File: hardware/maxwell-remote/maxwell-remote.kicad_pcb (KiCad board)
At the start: 2 copper layers, 71.1 x 38.1 mm, 28 parts, among them J2 UART, J3 FPC 1, J4 FPC 2, J5 Programmer, J6 B0_JMP, J7 B1_JMP, J9 ESP_BM, U1 STM32F103C8Tx, U2 ESP32-WROOM, Y1 Crystal, Y2 Crystal_GND23

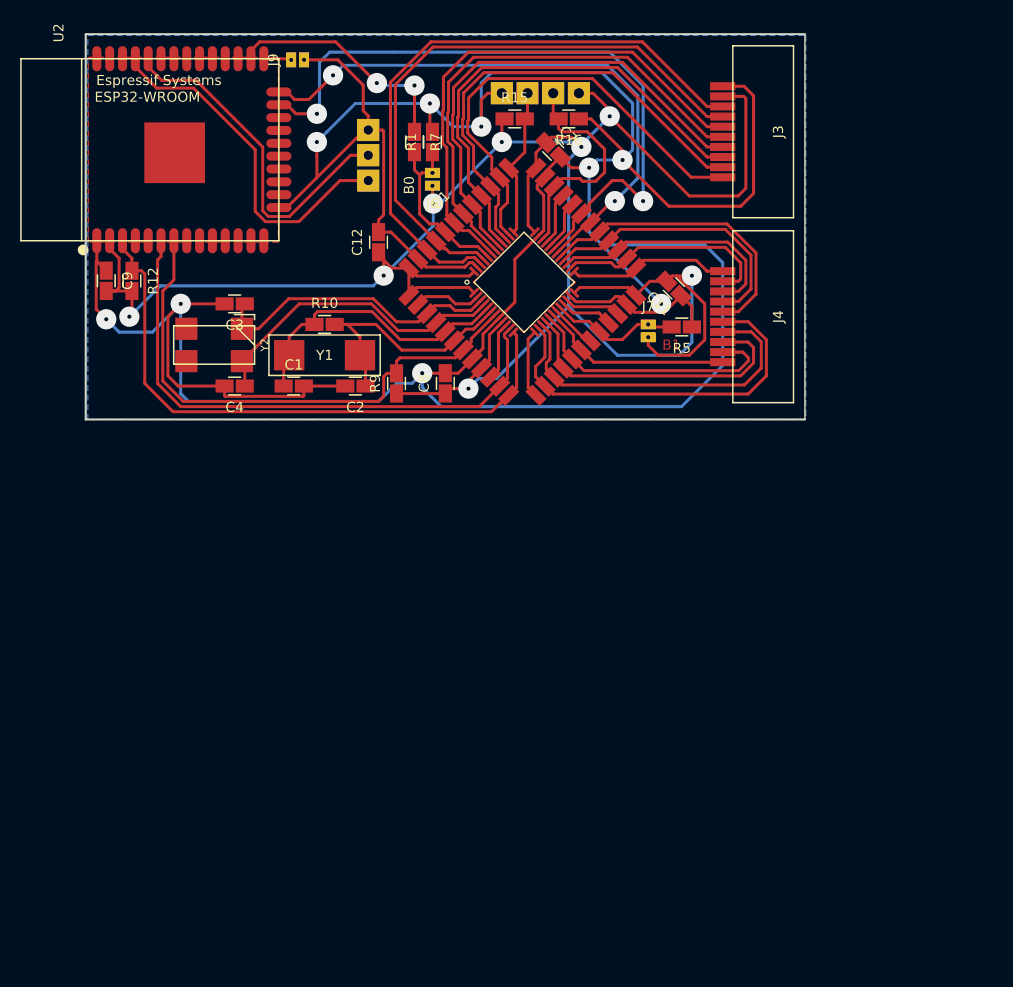
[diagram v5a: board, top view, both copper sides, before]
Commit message: Maxwell Remote v2.0
* Adds WAKE-controlled power switch to save power while sleeping.
* Uses pin headers for connecting upper and lower layers instead
  of FPC connectors.
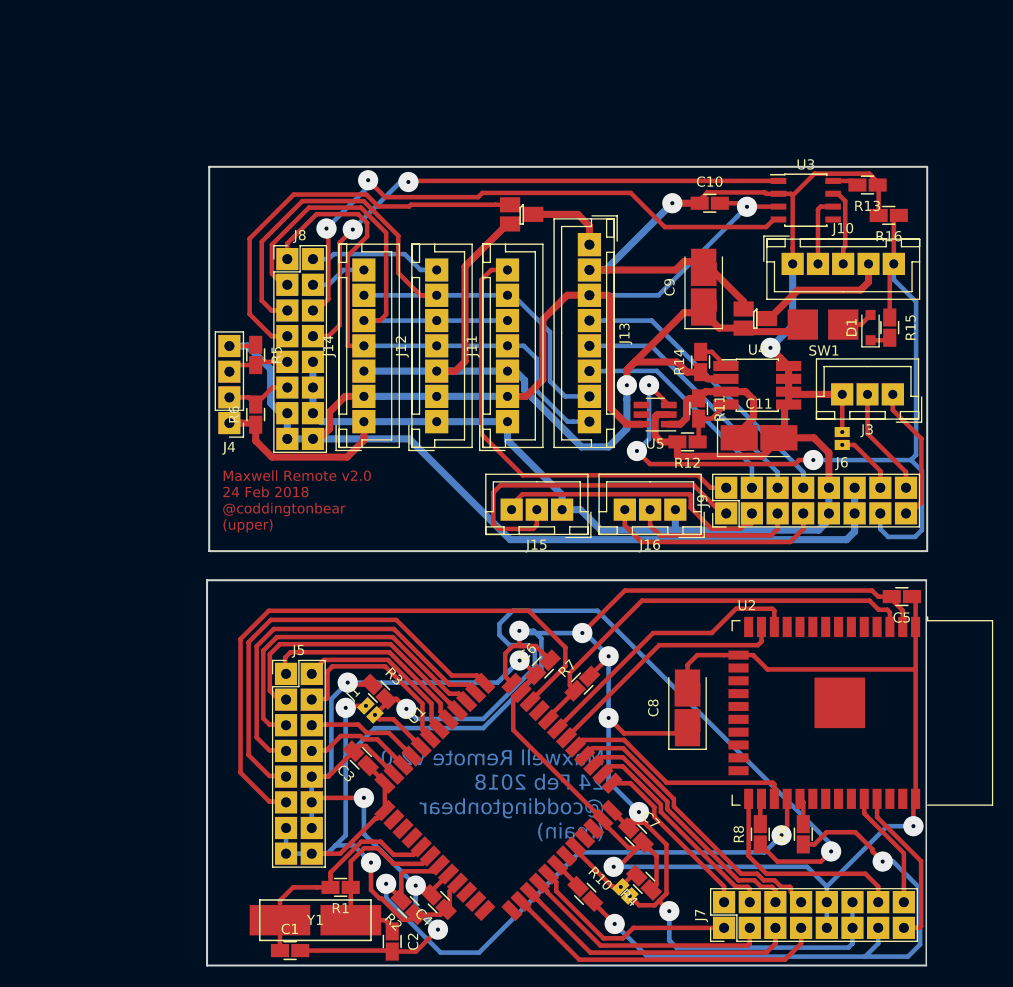
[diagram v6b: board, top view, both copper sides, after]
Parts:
- removed C12: 0.1, coddingtonbear/coddingtonbear.pretty:0805_Milling
- removed Y2: Crystal_GND23, coddingtonbear:SM-CRYSTAL-ABS25_LargePads
- added C10: 0.1u, coddingtonbear:0805_Milling, F.Cu at (159.5, 72.6)
- added C5: 0.1u, coddingtonbear:0805_Milling, F.Cu at (178.5, 111.5)
- added C6: 0.1u, coddingtonbear:0805_Milling, F.Cu at (143.0, 118.5)
- added D1: 1N4148WS, Diode_SMD:D_SOD-323_HandSoldering, F.Cu at (175.4, 84.9)
- added J1: BOOT0, coddingtonbear:Pin_Header_Straight_1x02_Pitch1.27mm_JMP, F.Cu at (125.5, 122.3)
- added J10: CAN, coddingtonbear:JST_XH_B05B-XH-A_05x2.50mm_Straight_LargePads, F.Cu at (167.7, 78.6)
- added J11: SPI1_C, coddingtonbear:JST_XH_B07B-XH-A_07x2.50mm_Straight_LargePads, F.Cu at (139.5, 94.2)
- added J12: SPI1_B, coddingtonbear:JST_XH_B07B-XH-A_07x2.50mm_Straight_LargePads, F.Cu at (132.5, 94.2)
- added J13: Display, coddingtonbear:JST_XH_B08B-XH-A_08x2.50mm_Straight_LargePads, F.Cu at (147.6, 76.7)
- added J14: SPI1_A, coddingtonbear:JST_XH_B07B-XH-A_07x2.50mm_Straight_LargePads, F.Cu at (125.3, 94.2)
- added J15: Left, coddingtonbear:JST_XH_B03B-XH-A_03x2.50mm_Straight_LargePads, F.Cu at (144.9, 102.9)
- added J16: Right, coddingtonbear:JST_XH_B03B-XH-A_03x2.50mm_Straight_LargePads, F.Cu at (156.1, 102.9)
- added J8: Upper-Left, coddingtonbear:PinHeader_2x08_P2.54mm_Vertical_LargePads, F.Cu at (117.7, 78.1)
- added Q1: NTR1P02TI, coddingtonbear:SOT-23_LargePads, F.Cu at (164.0, 84.0)
- added Q2: NTR1P02TI, coddingtonbear:SOT-23_LargePads, F.Cu at (140.9, 73.7)
- added R11: 60k, coddingtonbear:0805_Milling, F.Cu at (158.4, 92.9)
- added R13: 10k, coddingtonbear:0805_Milling, F.Cu at (175.1, 70.8)
- added R14: 10k, coddingtonbear:0805_Milling, F.Cu at (158.6, 88.3)
- added R2: 10k, coddingtonbear:0805_Milling, F.Cu at (129.7, 142.2)
- added R3: 100k, coddingtonbear:0805_Milling, F.Cu at (126.8, 120.9)
- added R4: 100k, coddingtonbear:0805_Milling, F.Cu at (153.0, 139.8)
- added R6: 10k, coddingtonbear:0805_Milling, F.Cu at (114.6, 93.5)
- added R8: 300, coddingtonbear:0805_Milling, F.Cu at (164.5, 135.0)
- added SW1: SW_Push, coddingtonbear:SMD_MINI_BLACK_TACTILE_SWITCH, F.Cu at (170.7, 84.6)
- added U3: SN65HVD235, Package_SO:SOIC-8_3.9x4.9mm_P1.27mm, F.Cu at (169.0, 72.3)
- added U4: MIC5209-ADJ, coddingtonbear:SOIC-8_3.9x4.9mm_P1.27mm_LargePads, F.Cu at (164.2, 90.6)
- added U5: TPS22917, Package_TO_SOT_SMD:SOT-23-6_Handsoldering, F.Cu at (154.1, 93.5)
- C1, C2, R16: footprint coddingtonbear/coddingtonbear.pretty:0805_Milling -> coddingtonbear:0805_Milling
- C11: value 0.1 -> 2.2u; footprint coddingtonbear/coddingtonbear.pretty:0805_Milling -> coddingtonbear:CP_Tantalum_Case-C_EIA-6032-28_Milling
- C3, C4: value 22p -> 0.1u; footprint coddingtonbear/coddingtonbear.pretty:0805_Milling -> coddingtonbear:0805_Milling
- C7: value 0.1 -> 0.1u; footprint coddingtonbear/coddingtonbear.pretty:0805_Milling -> coddingtonbear:0805_Milling
- C8: value 0.1 -> 220u; footprint coddingtonbear/coddingtonbear.pretty:0805_Milling -> coddingtonbear:CP_Tantalum_Case-C_EIA-6032-28_Milling
- C9: value 0.1 -> 100u; footprint coddingtonbear/coddingtonbear.pretty:0805_Milling -> coddingtonbear:CP_Tantalum_Case-C_EIA-6032-28_Milling
- J2: value UART -> BOOT1; footprint coddingtonbear:JST_XH_B03B-XH-A_03x2.50mm_Straight_LargePads -> coddingtonbear:Pin_Header_Straight_1x02_Pitch1.27mm_JMP
- J3: value FPC 1 -> ESPUART; footprint coddingtonbear/coddingtonbear.pretty:10P_FPC_1.0mm -> coddingtonbear:JST_XH_B03B-XH-A_03x2.50mm_Straight_LargePads
- J4: value FPC 2 -> PROG; footprint coddingtonbear/coddingtonbear.pretty:10P_FPC_1.0mm -> coddingtonbear:Pin_Header_Straight_1x04_Pitch2.54mm_LargePads
- J5: value Programmer -> Lower-Left; footprint coddingtonbear/coddingtonbear.pretty:Pin_Header_Straight_1x04_Pitch2.54mm_LargePads -> coddingtonbear:PinHeader_2x08_P2.54mm_Vertical_LargePads; moved to F.Cu
- J6: value B0_JMP -> ESPBOOT; footprint coddingtonbear/coddingtonbear.pretty:Pin_Header_Straight_1x02_Pitch1.27mm_JMP -> coddingtonbear:Pin_Header_Straight_1x02_Pitch1.27mm_JMP
- J7: value B1_JMP -> Lower-Right; footprint coddingtonbear/coddingtonbear.pretty:Pin_Header_Straight_1x02_Pitch1.27mm_JMP -> coddingtonbear:PinHeader_2x08_P2.54mm_Vertical_LargePads
- J9: value ESP_BM -> Upper-Right; footprint coddingtonbear/coddingtonbear.pretty:Pin_Header_Straight_1x02_Pitch1.27mm_JMP -> coddingtonbear:PinHeader_2x08_P2.54mm_Vertical_LargePads
- R1: value 100k -> 1M; footprint coddingtonbear/coddingtonbear.pretty:0805_Milling -> coddingtonbear:0805_Milling
- R10: value 1M -> 300; footprint coddingtonbear/coddingtonbear.pretty:0805_Milling -> coddingtonbear:0805_Milling
- R12: value 10k -> 100k; footprint coddingtonbear/coddingtonbear.pretty:0805_Milling -> coddingtonbear:0805_Milling
- R15, R9: value 10k -> 300; footprint coddingtonbear/coddingtonbear.pretty:0805_Milling -> coddingtonbear:0805_Milling
- R5: value 100k -> 10k; footprint coddingtonbear/coddingtonbear.pretty:0805_Milling -> coddingtonbear:0805_Milling
- R7: value 330 -> 10k; footprint coddingtonbear/coddingtonbear.pretty:0805_Milling -> coddingtonbear:0805_Milling
- U1: value STM32F103C8Tx -> STM32F103CBTx; footprint kicad-castellated-breakouts:QFP48-1.27MM-CASTELLATED-VERS -> castellated-breakouts:QFP48-1.27MM-CASTELLATED
- U2: value ESP32-WROOM -> ESP32-WROOM-32; footprint NorbotNorway/NorBotKiCadFootprints.pretty:ESP32-WROOM -> RF_Module:ESP32-WROOM-32
- Y1: value Crystal -> 8M; footprint cpavlina/kicad-pcblib/smd-non-ipc.pretty:Abracon-ABM2 -> coddingtonbear:Abracon-ABM2_LargePads
- moved U2 87.5 mm to (171.6, 123.0)
- moved R1 74.3 mm to (123.0, 140.2), turned to 180 degrees
- moved J2 74.2 mm to (150.7, 140.2), turned to 225 degrees
- moved C7 68.3 mm to (152.2, 135.1)
- moved J5 64.3 mm to (117.6, 119.1), turned to 0 degrees
- moved J9 62.1 mm to (161.1, 103.3)
- moved R10 61.9 mm to (147.2, 140.9), turned to 315 degrees
- moved J7 60.1 mm to (160.9, 144.3), turned to 90 degrees
- moved R9 60.0 mm to (168.8, 135.0)
- moved C9 59.1 mm to (158.9, 80.9), turned to 90 degrees
- moved R12 57.2 mm to (157.3, 96.2), turned to 180 degrees
- moved R7 56.1 mm to (146.9, 120.1), turned to 45 degrees
- moved Y1 55.9 mm to (120.5, 143.5), turned to 0 degrees
- moved C1 55.8 mm to (118.0, 146.5)
- moved C2 55.0 mm to (128.1, 145.6), turned to 270 degrees
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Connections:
- C1 pad 2: GND -> GND_A
- C11 pad 1: GND -> +3V3_U
- C11 pad 2: +3V3 -> GND_B
- C2 pad 2: GND -> GND_A
- C3 pad 1: Net-(C3-Pad1) -> +3V3_A
- C3 pad 2: GND -> GND_A
- C4 pad 1: Net-(C4-Pad1) -> +3V3_A
- C4 pad 2: GND -> GND_A
- C7 pad 1: +3V3 -> +3V3_A
- C7 pad 2: GND -> GND_A
- C8 pad 1: +3V3 -> +3V3_A
- C8 pad 2: GND -> GND_A
- C9 pad 1: GND -> +BATT
- C9 pad 2: +3V3 -> GND_B
- J2 pad 1: BT_OUT -> BOOT1
- J2 pad 2: BT_IN -> +3V3_A
- J3 pad 1: GND -> ESP_DO_U
- J3 pad 2: +3V3 -> ESP_DI_U
- J3 pad 3: CAN_TX -> GND_B
- J4 pad 1: ~SPI_CS_4 -> GND_B
- J4 pad 2: SCREEN_A0 -> SWDIO_U
- J4 pad 3: ~SCREEN_RST -> SWCLK_U
- J4 pad 4: ~SCREEN_CS -> +3V3_B
- J5 pad 1: +3V3 -> SPI1_MOSI
- J5 pad 2: SWDIO -> ~SPI1_CS_3
- J5 pad 3: SWCLK -> SPI1_MISO
- J5 pad 4: GND -> ~SPI1_CS_2
- J6 pad 1: +3V3 -> ESP_BOOT_MODE_U
- J6 pad 2: BOOT0 -> GND_B
- J7 pad 1: BOOT1 -> ~LEFT_A
- J7 pad 2: +3V3 -> ~SPI_CS_4
- J9 pad 1: ESP_BOOT_MODE -> LEFT_A_U
- J9 pad 2: GND -> ~SPI1_CS_4_U
- R1 pad 1: BOOT0 -> Net-(C2-Pad1)
- R1 pad 2: GND -> Net-(C1-Pad1)
- R10 pad 1: Net-(C1-Pad1) -> Net-(R10-Pad1)
- R10 pad 2: Net-(C2-Pad1) -> ESP_AVAILABLE
- R12 pad 1: DISBABLE_BLUETOOTH_ -> Net-(R11-Pad2)
- R12 pad 2: +3V3 -> GND_B
- R15 pad 1: +3V3 -> ESP_AVAILABLE_U
- R15 pad 2: SWCLK -> Net-(D1-Pad1)
- R16 pad 1: GND -> ESP_AVAILABLE_U
- R16 pad 2: SWDIO -> GND_B
- R5 pad 1: GND -> +3V3_B
- R5 pad 2: BOOT1 -> SWCLK_U
- R7 pad 1: Net-(R7-Pad1) -> DISBABLE_BLUETOOTH_
- R7 pad 2: BOOT0 -> +3V3_A
- R9 pad 1: +3V3 -> ESP_AVAILABLE
- R9 pad 2: NRST -> Net-(R9-Pad2)
- U1 pad 1: +3V3 -> +3V3_A
- U1 pad 11: BT_KEY -> Net-(U1-Pad11)
- U1 pad 12: DISBABLE_BLUETOOTH_ -> Net-(U1-Pad12)
- U1 pad 18: WAKE -> Net-(R10-Pad1)
- U1 pad 23: GND -> GND_A
- U1 pad 24: +3V3 -> +3V3_A
- U1 pad 29: ~ENABLE_CAN -> BT_KEY
- U1 pad 3: Net-(C3-Pad1) -> Net-(U1-Pad3)
- U1 pad 30: MC_OUT -> BT_DI
- U1 pad 31: MC_IN -> BT_DO
- U1 pad 32: Net-(U1-Pad32) -> DISBABLE_BLUETOOTH_
- U1 pad 35: GND -> GND_A
- U1 pad 36: +3V3 -> +3V3_A
- U1 pad 4: Net-(C4-Pad1) -> Net-(U1-Pad4)
- U1 pad 47: GND -> GND_A
- U1 pad 48: +3V3 -> +3V3_A
- U1 pad 8: GND -> GND_A
- U1 pad 9: +3V3 -> +3V3_A
- U2 pad 1: GND -> GND_A
- U2 pad 12: Net-(U2-Pad12) -> BT_DO
- U2 pad 13: Net-(U2-Pad13) -> BT_DI
- U2 pad 15: GND -> GND_A
- U2 pad 2: +3V3 -> +3V3_A
- U2 pad 23: MC_IN -> Net-(U2-Pad23)
- U2 pad 24: MC_OUT -> Net-(U2-Pad24)
- U2 pad 26: Net-(R7-Pad1) -> Net-(R8-Pad2)
- U2 pad 27: Net-(U2-Pad27) -> BT_KEY
- U2 pad 28: Net-(U2-Pad28) -> NRST
- U2 pad 29: Net-(U2-Pad29) -> Net-(R9-Pad2)
- U2 pad 34: BT_IN -> ESP_DI
- U2 pad 35: BT_OUT -> ESP_DO
- U2 pad 38: GND -> GND_A
- U2 pad 39: GND -> (no net)
- U2 pad 6: BT_KEY -> Net-(U2-Pad6)
- U2 pad 7: NRST -> Net-(U2-Pad7)
- Y1 pad 1: Net-(C2-Pad1) -> Net-(C1-Pad1)
- Y1 pad 2: Net-(C1-Pad1) -> Net-(C2-Pad1)
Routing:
- net GND: track 350.5 -> 0.00 mm, vias 9 -> 0
- net +3V3: track 236.7 -> 0.00 mm, vias 8 -> 0
- net +3V3_A: track 0.00 -> 215.8 mm, vias 0 -> 8
- net GND_A: track 0.00 -> 209.6 mm, vias 0 -> 7
- net GND_B: track 0.00 -> 203.1 mm, vias 0 -> 2
- net +3V3_B: track 0.00 -> 160.2 mm, vias 0 -> 1
- net +BATT: track 0.00 -> 86.4 mm, vias 0 -> 1
- net ESP_AVAILABLE_U: track 0.00 -> 82.6 mm, vias 0 -> 3
- net MC_IN: track 67.7 -> 0.00 mm, vias 2 -> 0
- net BOOT0: track 18.3 -> 84.2 mm, vias 0 -> 2
- net SPI1_SCK_U: track 0.00 -> 63.0 mm
- net ESP_AVAILABLE: track 0.00 -> 58.8 mm, vias 0 -> 2
- net CAN_RX_U: track 0.00 -> 58.7 mm, vias 0 -> 2
- net MC_OUT: track 57.8 -> 0.00 mm, vias 2 -> 0
- net CAN_TX_U: track 0.00 -> 57.2 mm, vias 0 -> 2
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- removed copper zone on B.Cu, net GND
- removed copper zone on F.Cu, net GND
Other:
- board size 71.1 x 38.1 mm -> 71.2 x 79 mm
- net class Default: trace_width 0.3 -> 0.45
- board text added: "Maxwell Remote v2.0 24 Feb 2018 @coddingtonbear (main)"
- board text added: "Maxwell Remote v2.0 24 Feb 2018 @coddingtonbear (upper)"
- board text removed: "+"
- board text removed: "-"
- board text removed: "B0"
- board text removed: "B1"
- board text removed: "C"
- board text removed: "IO"
- board text removed: "RX"
- board text removed: "TX"
- board text removed: "_"
- board text removed: "maxwell-remote v5.0 @coddingtonbear 24 June 2018"

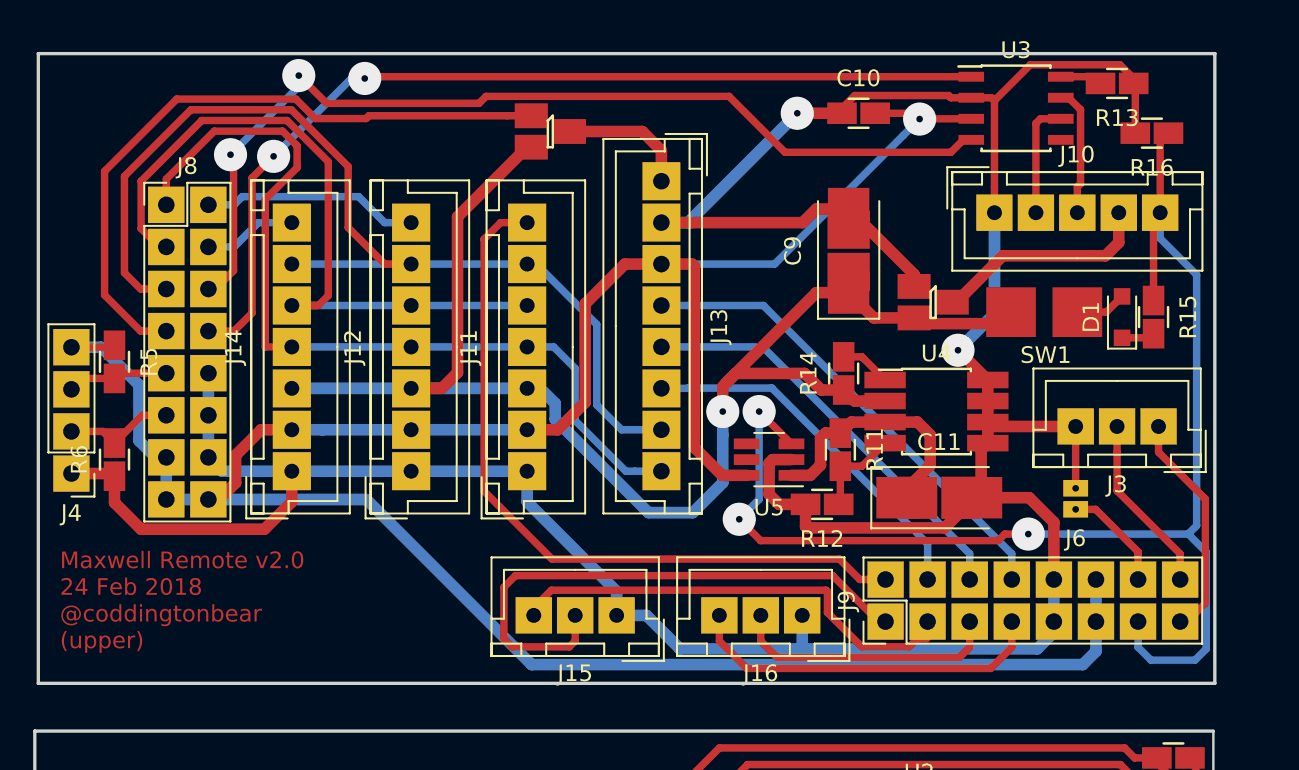
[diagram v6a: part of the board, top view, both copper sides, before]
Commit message: Maxwell Remote v2.0.1
* Adds support for power-on by pressing handlebar button.
  The earlier design relied on the microcontroller waking
  when the button was pressed, but in this new switch
  configuration the microcontroller won't even be powered
  while the device is asleep, so we need to hard-wire
  the power button to the WAKE line.
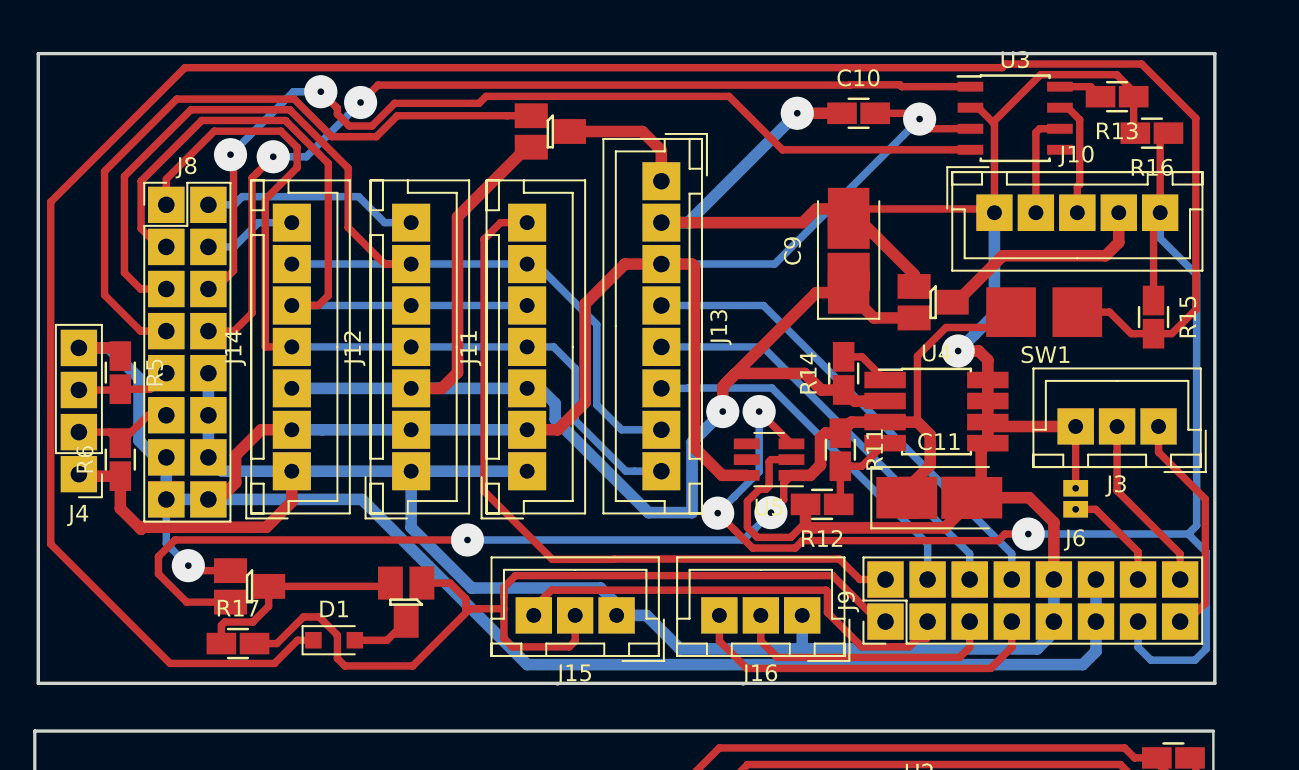
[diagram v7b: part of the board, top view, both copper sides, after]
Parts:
- added Q3: NTR1P02TI, coddingtonbear:SOT-23_LargePads, F.Cu at (122.8, 101.2)
- added Q4: NTR1P02TI, coddingtonbear:SOT-23_LargePads, F.Cu at (132.2, 102.1)
- added R17: 10k, coddingtonbear:0805_Milling, F.Cu at (122.0, 104.6)
- moved D1 51.4 mm to (127.8, 104.4), turned to 0 degrees
- moved R13 0.80 mm to (175.1, 71.6)
- moved R5 0.74 mm to (115.0, 88.2)
- moved U3 0.60 mm to (168.9, 72.9)
- moved J4 0.45 mm to (112.5, 94.4)
- moved R6 0.35 mm to (115.0, 93.5)
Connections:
- SW1 pad 1: +BATT -> +3V3_U
- SW1 pad 2: Net-(D1-Pad2) -> Net-(D1-Pad1)
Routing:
- net Net-(D1-Pad1): track 2.00 -> 133.8 mm
- net +3V3_U: track 15.6 -> 73.3 mm, vias 0 -> 2
- net LEFT_A_U: track 33.8 -> 56.9 mm
- net Net-(Q3-Pad3): track 0.00 -> 13.1 mm
- net GND_B: track 203.1 -> 215.7 mm
- net +3V3_B: track 160.2 -> 167.4 mm, vias 1 -> 2
- net +BATT: track 86.4 -> 80.1 mm
- net ESP_AVAILABLE_U: track 82.6 -> 84.6 mm
- net ~ENABLE_SCREEN_U: track 40.2 -> 41.1 mm
- net Net-(J10-Pad3): track 7.79 -> 7.17 mm
- net Net-(J10-Pad2): track 7.00 -> 6.38 mm
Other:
- board text removed: "Maxwell Remote v2.0 24 Feb 2018 @coddingtonbear (upper)"

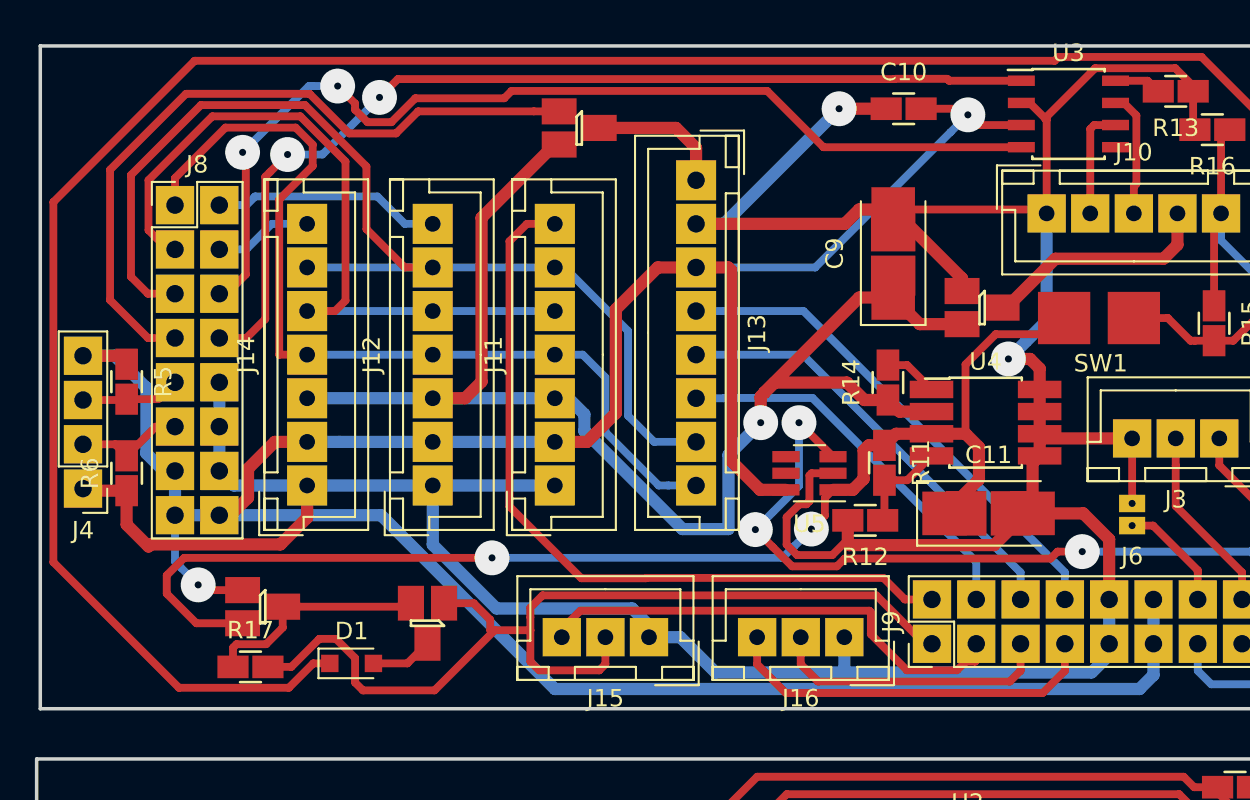
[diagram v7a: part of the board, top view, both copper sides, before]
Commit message: Maxwell Remote v2.0.2
* Switches off power to SPI-connected devices when powered-down.
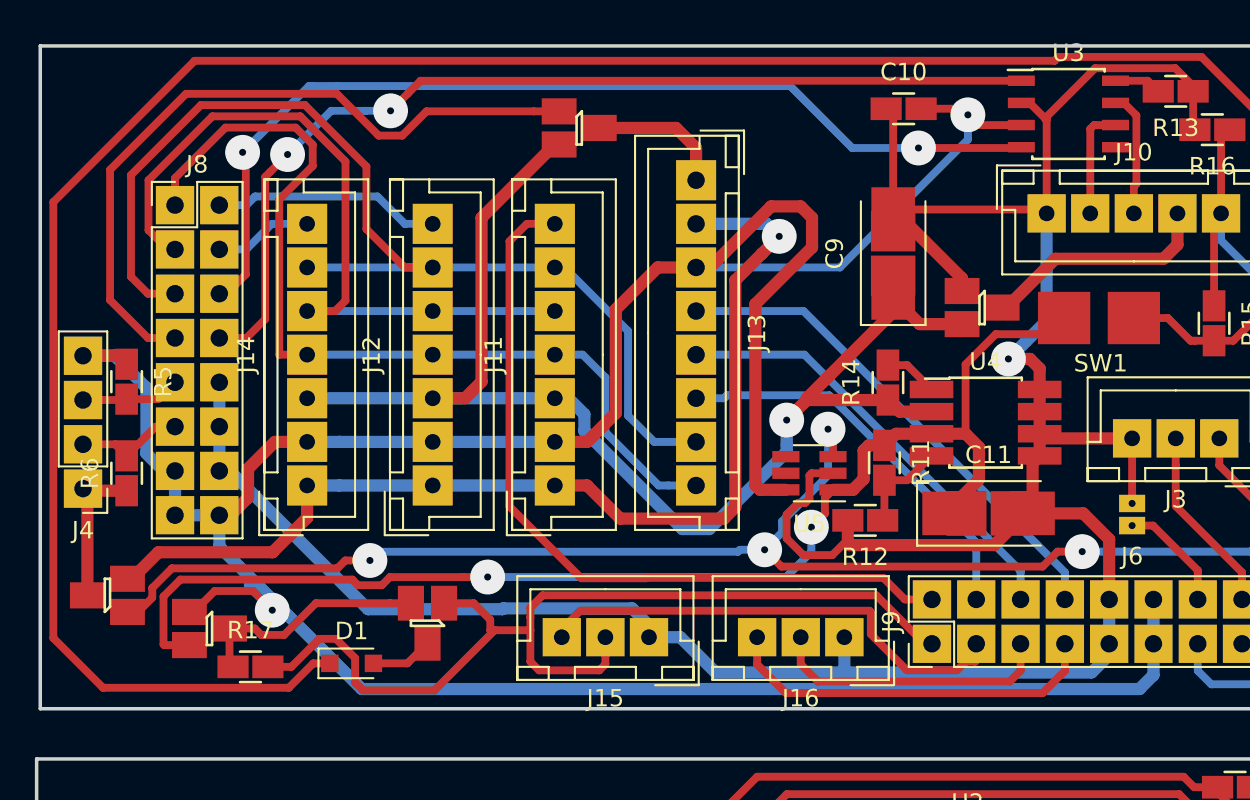
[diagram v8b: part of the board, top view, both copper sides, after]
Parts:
- added Q5: NTR1P02TI, coddingtonbear:SOT-23_LargePads, F.Cu at (113.8, 100.5)
- moved Q3 3.30 mm to (119.7, 102.4)
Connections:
- J11 pad 1: GND_B -> Net-(J11-Pad1)
- J12 pad 1: GND_B -> Net-(J11-Pad1)
- J13 pad 2: GND_B -> Net-(J11-Pad1)
- J14 pad 1: GND_B -> Net-(J11-Pad1)
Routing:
- net Net-(J11-Pad1): track 0.00 -> 60.8 mm, vias 0 -> 1
- net GND_B: track 215.7 -> 178.0 mm, vias 2 -> 1
- net ESP_AVAILABLE_U: track 84.6 -> 122.2 mm, vias 3 -> 4
- net +3V3_B: track 167.4 -> 180.5 mm
- net +BATT: track 80.1 -> 76.5 mm
- net Net-(D1-Pad1): track 133.8 -> 136.4 mm
- net CAN_RX_U: track 58.4 -> 56.8 mm
- net SCREEN_AO_U: track 22.1 -> 22.9 mm
- net Net-(Q3-Pad3): track 13.1 -> 13.6 mm
